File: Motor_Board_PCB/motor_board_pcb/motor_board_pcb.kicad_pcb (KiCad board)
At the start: 2 copper layers, 95 x 45 mm, 110 parts, among them J1 CAN_OUT, J11 CSP-USC16-TR, J2 Screw_Terminal_01x04, J3 Conn_01x02, J4 Screw_Terminal_01x06, J5 Screw_Terminal_01x04, J6 Conn_01x03, J8 Conn_01x02, U1 R7FA4M1AB3CFM, U2 MCP2515-xST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

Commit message: Meeting layout updates
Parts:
- added R34: 0, Resistor_SMD:R_0402_1005Metric, F.Cu at (158.2, 82.8)
- added R35: 0, Resistor_SMD:R_0402_1005Metric, F.Cu at (158.2, 83.9)
- added R36: 0, Resistor_SMD:R_0402_1005Metric, F.Cu at (137.7, 82.0)
- added R7: 0, Resistor_SMD:R_0402_1005Metric, F.Cu at (158.1, 81.2)
- moved TP5 14.3 mm to (131.7, 76.0)
- moved TP13 14.0 mm to (151.2, 88.0)
- moved C14 12.5 mm to (127.1, 90.3)
- moved U3 12.5 mm to (122.0, 90.3)
- moved D11 11.8 mm to (180.8, 74.5)
- moved J8 11.8 mm to (185.3, 77.1)
- moved TP3 10.5 mm to (131.7, 78.0)
- moved TP11 10.0 mm to (149.2, 88.0)
- moved TP2 7.94 mm to (177.1, 72.5)
- moved D6 7.12 mm to (120.9, 79.5)
- moved D7 7.12 mm to (120.8, 76.7)
- moved R17 7.12 mm to (125.1, 79.3)
- moved R18 7.12 mm to (125.0, 76.4)
- moved TP12 6.09 mm to (147.2, 88.0)
- moved C11 3.95 mm to (136.4, 95.7)
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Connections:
- U1 pad 34: D11 -> Net-(U1-CTX0/TDO/SWO/GTIOC1A/P109)
- U1 pad 36: D13 -> Net-(U1-GTIOC3A/P111)
- U1 pad 37: D10 -> Net-(U1-GTIOC3B/P112)
- U2 pad 17: D12 -> Net-(U2-SO)
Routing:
- net +5V: track 237.2 -> 215.9 mm, vias 9 -> 11
- net /CAN/CAN_LOW: track 11.9 -> 24.4 mm
- net /CAN/CAN_HI: track 11.9 -> 24.5 mm
- net D12: track 40.8 -> 29.8 mm
- net D13: track 39.6 -> 29.5 mm
- net D11: track 42.4 -> 32.4 mm
- net D10: track 38.4 -> 31.7 mm
- net VUSB: track 24.5 -> 29.0 mm, vias 2 -> 3
- net Net-(U2-SO): track 0.00 -> 4.25 mm
- net Net-(U1-CTX0/TDO/SWO/GTIOC1A/P109): track 0.00 -> 3.68 mm
- net Net-(U1-GTIOC3A/P111): track 0.00 -> 3.38 mm
- net Net-(U1-GTIOC3B/P112): track 0.00 -> 3.17 mm
- net Net-(D7-K): track 27.8 -> 30.4 mm, vias 2 -> 0
- net USB_D-: track 17.9 -> 19.8 mm
- net USB_D+: track 18.4 -> 19.4 mm
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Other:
- board text added: "FYDP 2024 Group 26 - Ethan Gilbert - Brandon Phu - Jonathon Ko - Ben Flack"

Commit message: Jonathan spelling fix
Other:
- board text added: "FYDP 2024 Group 26 - Ethan Gilbert - Brandon Phu - Jonathan Ko - Ben Flack"
- board text removed: "FYDP 2024 Group 26 - Ethan Gilbert - Brandon Phu - Jonathon Ko - Ben Flack"
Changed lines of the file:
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@@
   (gr_rect (start 92.3 57.9) (end 187.3 102.9)
     (stroke (width 0.1) (type default)) (fill none) (layer "Edge.Cuts"))
-  (gr_text "FYDP 2024\nGroup 26\n- Ethan Gilbert\n- Brandon Phu\n- Jonathon Ko\n- Ben Flack" (at 116.13 100.99) (layer "B.SilkS")
+  (gr_text "FYDP 2024\nGroup 26\n- Ethan Gilbert\n- Brandon Phu\n- Jonathan Ko\n- Ben Flack" (at 116.13 100.99) (layer "B.SilkS")
     (effects (font (size 1.5 1.5) (thickness 0.3) bold) (justify left bottom mirror))
   )

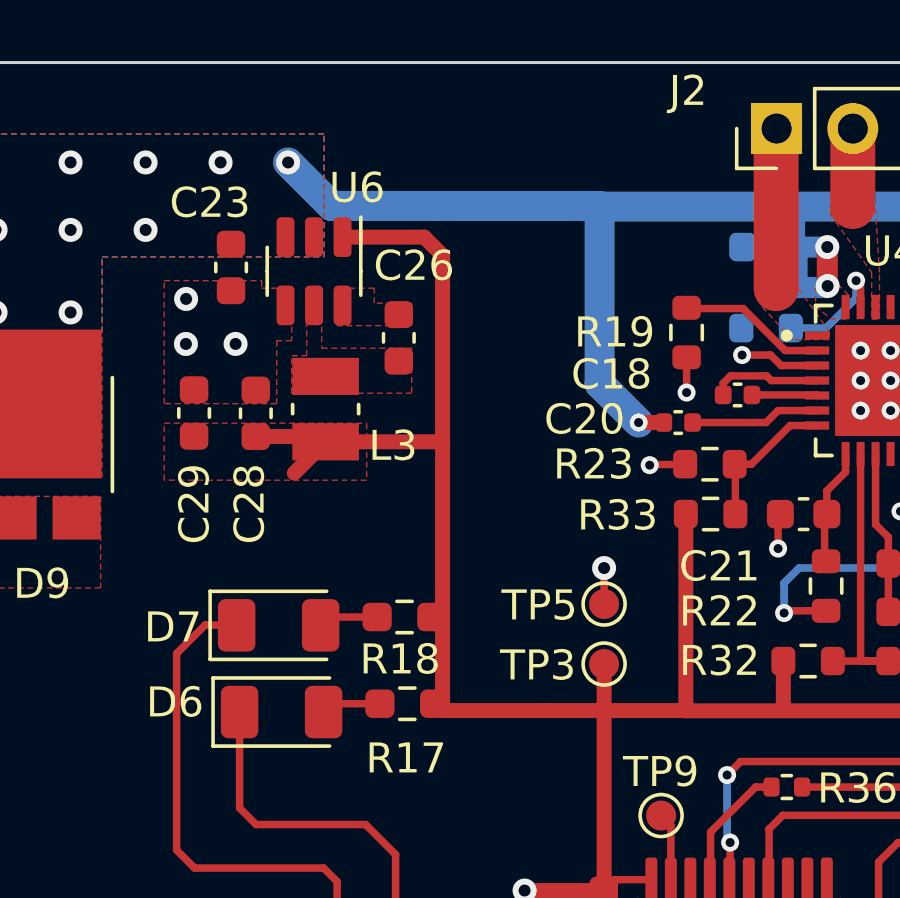
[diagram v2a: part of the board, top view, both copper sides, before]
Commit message: Testpoint location changes
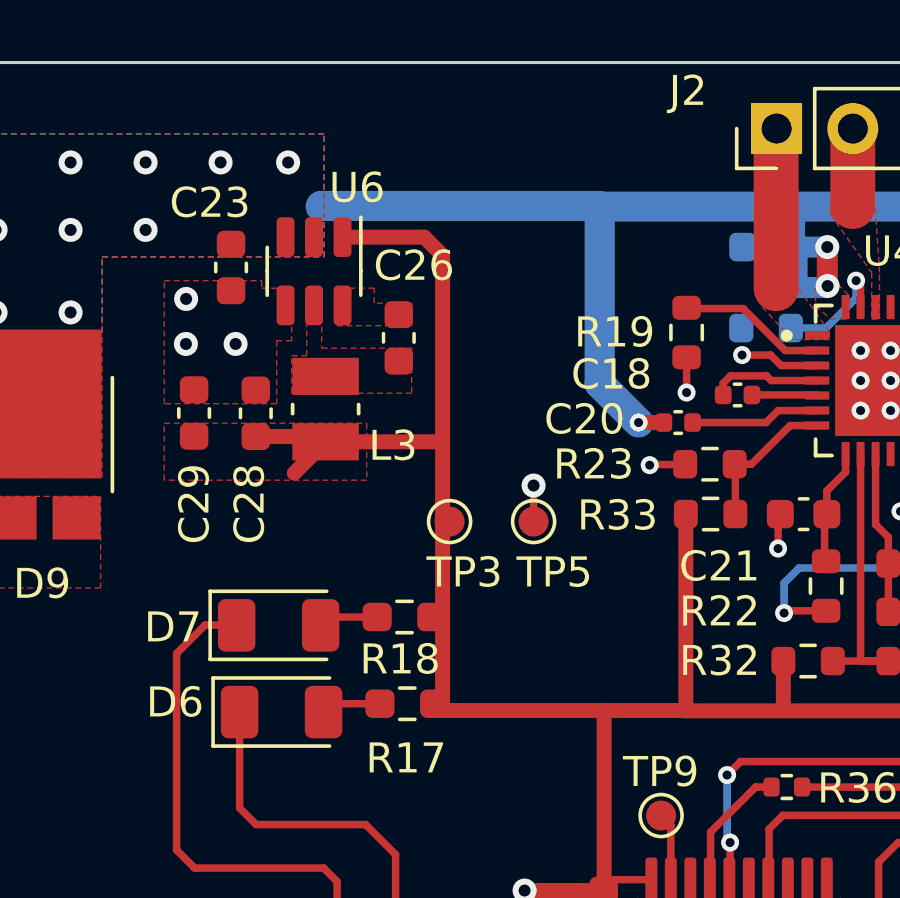
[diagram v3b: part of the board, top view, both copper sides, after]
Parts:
- moved TP3 7.01 mm to (126.5, 73.2)
- moved TP5 3.62 mm to (129.3, 73.2)
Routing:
- net +12V: track 45.8 -> 44.1 mm
- net +5V: track 215.9 -> 214.3 mm
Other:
- board text added: "ECE FYDP 2024 Group 26 - Ethan Gilbert - Brandon Phu - Jonathan Ko - Ben Flack"
- board text removed: "FYDP 2024 Group 26 - Ethan Gilbert - Brandon Phu - Jonathan Ko - Ben Flack"
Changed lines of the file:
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@@
   )
   (footprint "TestPoint:TestPoint_Pad_D1.0mm" (layer "F.Cu")
-    (at 131.65 77.95)
+    (at 126.5 73.2)
     (descr "SMD pad as test Point, diameter 1.0mm")
     (tags "test point SMD pad")
@@
     (property "ki_keywords" "test point tp")
     (attr exclude_from_pos_files)
-    (fp_text reference "TP3" (at -2.2 0.05) (layer "F.SilkS")
+    (fp_text reference "TP3" (at 0.5 1.7) (layer "F.SilkS")
         (effects (font (size 1 1) (thickness 0.16)))
     )
@@
   )
   (footprint "TestPoint:TestPoint_Pad_D1.0mm" (layer "F.Cu")
-    (at 131.65 75.95)
+    (at 129.3 73.2)
     (descr "SMD pad as test Point, diameter 1.0mm")
     (tags "test point SMD pad")
@@
     (property "ki_keywords" "test point tp")
     (attr exclude_from_pos_files)
-    (fp_text reference "TP5" (at -2.15 0.05) (layer "F.SilkS")
+    (fp_text reference "TP5" (at 0.7 1.7) (layer "F.SilkS")
         (effects (font (size 1 1) (thickness 0.16)))
     )
@@
   (gr_rect (start 92.3 57.9) (end 187.3 102.9)
     (stroke (width 0.1) (type default)) (fill none) (layer "Edge.Cuts"))
-  (gr_text "FYDP 2024\nGroup 26\n- Ethan Gilbert\n- Brandon Phu\n- Jonathan Ko\n- Ben Flack" (at 116.13 100.99) (layer "B.SilkS")
+  (gr_text "ECE FYDP 2024\nGroup 26\n- Ethan Gilbert\n- Brandon Phu\n- Jonathan Ko\n- Ben Flack" (at 116.13 100.99) (layer "B.SilkS")
     (effects (font (size 1.5 1.5) (thickness 0.3) bold) (justify left bottom mirror))
   )
@@
   (segment (start 131.625 87.0509) (end 131.6384 87.0375) (width 0.25) (layer "F.Cu") (net 1))
   (segment (start 173.892173 64.76) (end 173.892173 65.821365) (width 0.25) (layer "F.Cu") (net 1))
-  (segment (start 131.65 74.75) (end 131.65 75.95) (width 0.25) (layer "F.Cu") (net 1))
+  (segment (start 129.3 72) (end 129.3 73.2) (width 0.25) (layer "F.Cu") (net 1))
   (segment (start 136.25 67.65) (end 137.2 67.65) (width 0.25) (layer "F.Cu") (net 1))
   (segment (start 175.3 83.2) (end 175.3 82.325) (width 0.25) (layer "F.Cu") (net 1))
@@
   (via (at 141.2 68.5) (size 0.6) (drill 0.3) (layers "F.Cu" "B.Cu") (net 1))
   (via (at 142.2 68.5) (size 0.6) (drill 0.3) (layers "F.Cu" "B.Cu") (net 1))
-  (via (at 131.65 74.75) (size 0.8) (drill 0.4) (layers "F.Cu" "B.Cu") (free) (net 1))
+  (via (at 129.3 72) (size 0.8) (drill 0.4) (layers "F.Cu" "B.Cu") (free) (net 1))
   (via (at 142.2 67.5) (size 0.6) (drill 0.3) (layers "F.Cu" "B.Cu") (net 1))
   (via (at 140.2 68.5) (size 0.6) (drill 0.3) (layers "F.Cu" "B.Cu") (net 1))
@@
   (segment (start 137.85 62.87) (end 138.02 62.7) (width 1) (layer "B.Cu") (net 11))
   (segment (start 137.85 64.025) (end 137.85 62.87) (width 1) (layer "B.Cu") (net 11))
-  (segment (start 131.48 62.68) (end 131.5 62.7) (width 1) (layer "B.Cu") (net 11))
+  (segment (start 122.2 62.7) (end 122.22 62.68) (width 1) (layer "B.Cu") (net 11))
   (segment (start 144.37 64.255) (end 144.625 64) (width 0.7) (layer "B.Cu") (net 11))
+  (segment (start 131.48 62.68) (end 131.5 62.7) (width 1) (layer "B.Cu") (net 11))
+  (segment (start 122.22 62.68) (end 131.48 62.68) (width 1) (layer "B.Cu") (net 11))
   (segment (start 144.575 64.05) (end 144.625 64) (width 0.25) (layer "B.Cu") (net 11))
   (segment (start 139.05 65.4) (end 139.1 65.35) (width 0.25) (layer "B.Cu") (net 11))
@@
   (segment (start 144.37 65.35) (end 144.37 64.255) (width 0.7) (layer "B.Cu") (net 11))
   (segment (start 138.08 64.305) (end 137.825 64.05) (width 0.7) (layer "B.Cu") (net 11))
-  (segment (start 121.116833 61.23) (end 122.566833 62.68) (width 1) (layer "B.Cu") (net 11))
   (segment (start 137.825 64.05) (end 139.09 64.05) (width 0.7) (layer "B.Cu") (net 11))
   (segment (start 138.02 62.7) (end 144.56 62.7) (width 1) (layer "B.Cu") (net 11))
-  (segment (start 122.566833 62.68) (end 131.48 62.68) (width 1) (layer "B.Cu") (net 11))
   (segment (start 144.37 65.35) (end 143.3 65.35) (width 0.7) (layer "B.Cu") (net 11))
   (segment (start 138.08 65.4) (end 139.05 65.4) (width 0.7) (layer "B.Cu") (net 11))
@@
   (segment (start 165.5 98.1) (end 165.6 98) (width 0.5) (layer "F.Cu") (net 18))
   (segment (start 129.75 79.5) (end 134.37 79.5) (width 0.5) (layer "F.Cu") (net 18))
-  (segment (start 131.65 79.5) (end 131.65 77.95) (width 0.5) (layer "F.Cu") (net 18))
   (segment (start 129 89.45) (end 127.19 89.45) (width 0.5) (layer "F.Cu") (net 18))
   (segment (start 131.6384 85.4875) (end 131.65 85.4759) (width 0.5) (layer "F.Cu") (net 18))

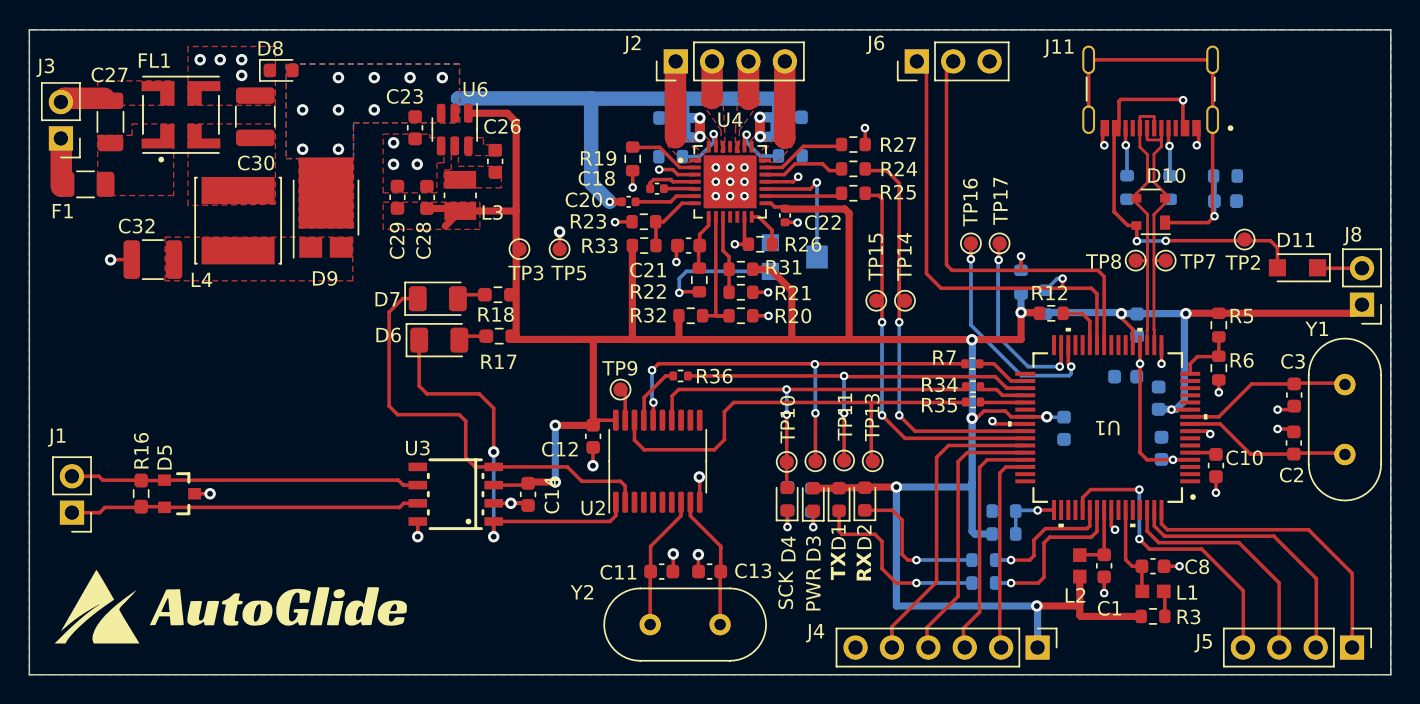
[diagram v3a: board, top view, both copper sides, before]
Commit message: All usb changes on both boards
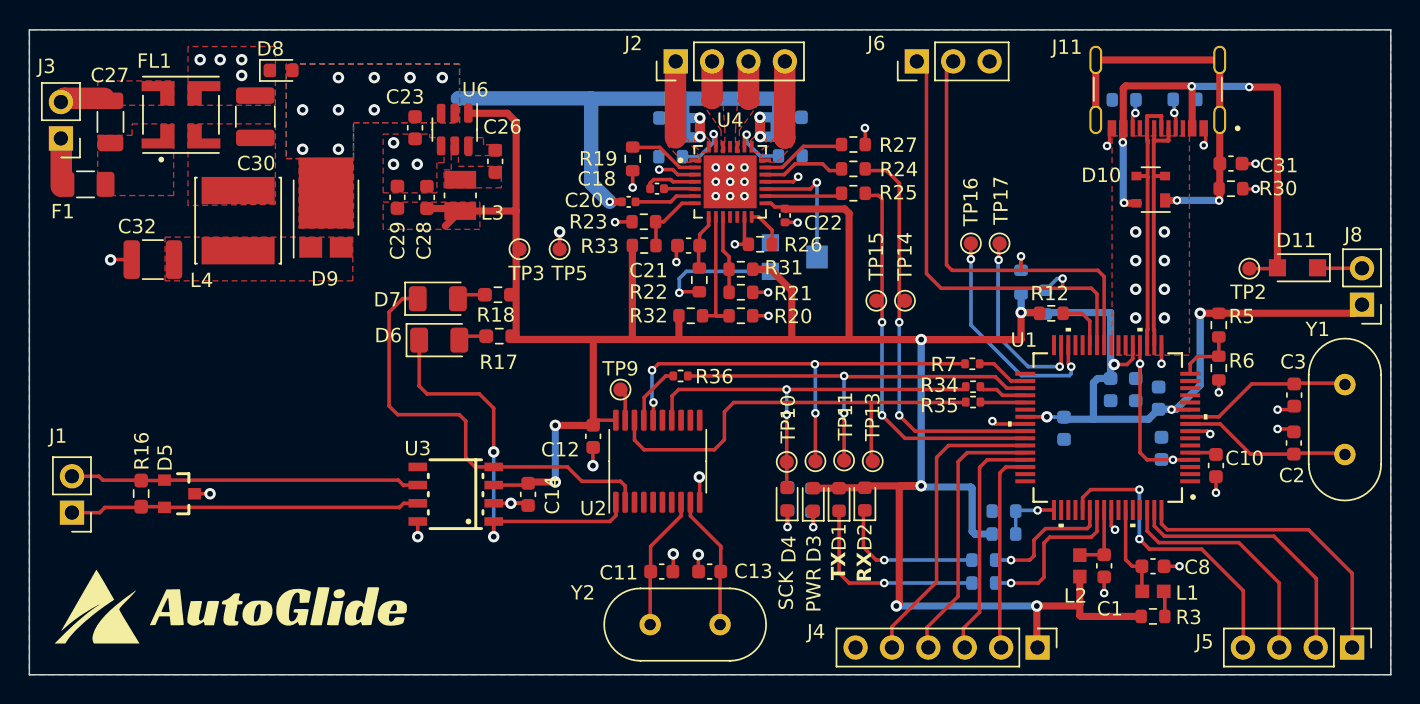
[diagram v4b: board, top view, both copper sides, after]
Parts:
- removed TP7, TP8: TestPoint, TestPoint:TestPoint_Pad_D1.0mm
- C31, R30: moved to F.Cu
- moved R2 6.24 mm to (172.9, 62.8), turned to 0 degrees
- moved R1 6.12 mm to (168.7, 62.8), turned to 180 degrees
- moved C5 4.87 mm to (167.8, 83.0)
- moved C31 2.65 mm to (176.1, 67.2)
- moved TP2 2.06 mm to (177.4, 74.6)
- moved D10 1.55 mm to (170.6, 69.0)
- moved C7 1.14 mm to (169.5, 83.0), turned to 90 degrees
- moved R30 0.96 mm to (176.1, 69.0)
- moved J11 0.50 mm to (171.0, 64.8)
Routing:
- net +5V: track 214.3 -> 224.9 mm
- net VUSB: track 29.0 -> 37.7 mm, vias 3 -> 4
- net /Connectors/SHIELD2: track 29.7 -> 26.4 mm, vias 1 -> 2
- net GND: track 45.4 -> 47.3 mm, vias 47 -> 57
- net USB_D-: track 19.8 -> 17.9 mm
- net CC1: track 3.52 -> 2.09 mm
- net CC2: track 3.37 -> 2.08 mm
- net USB_D+: track 19.4 -> 18.7 mm
- net Net-(D1-K): track 13.4 -> 13.9 mm

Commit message: Kim changes + GND pour + TearDrops + Oscillator changes
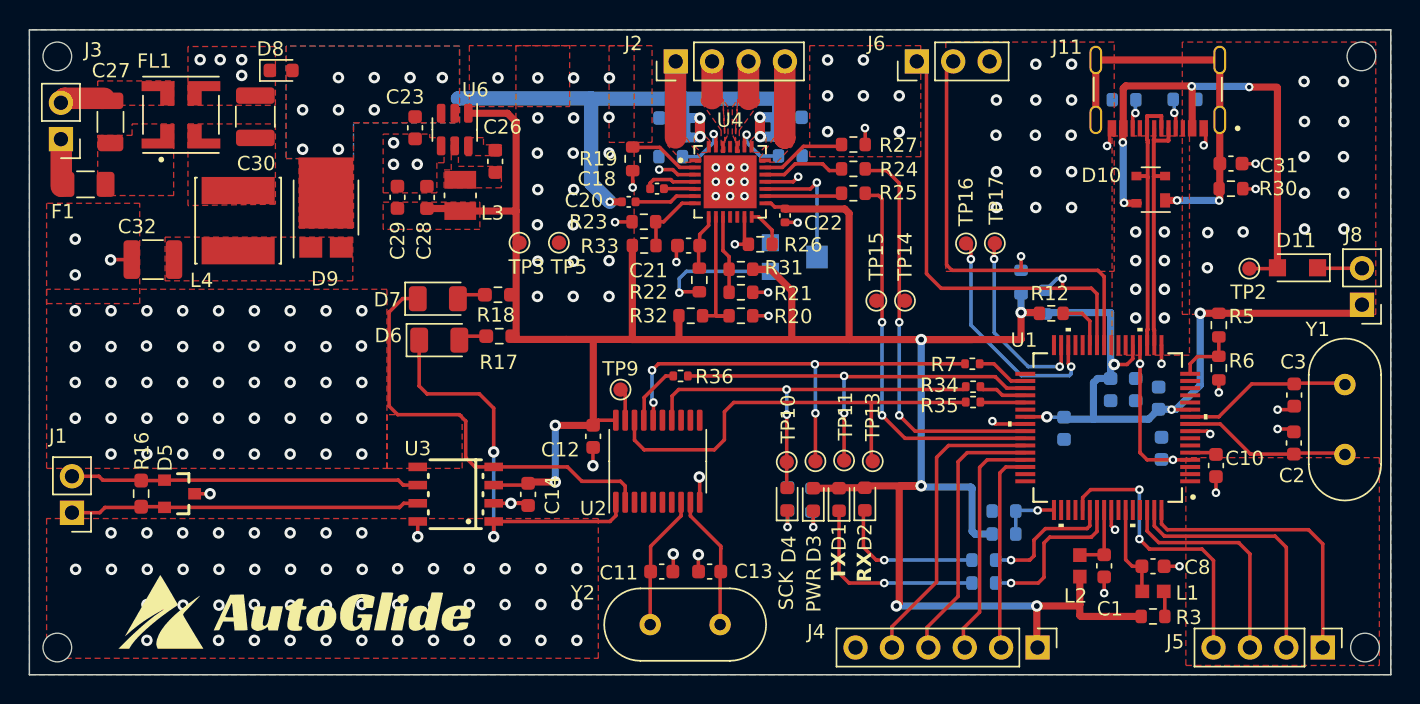
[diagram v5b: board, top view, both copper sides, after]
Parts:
- added ?: , , F.Cu at (94.2, 101.0)
- added ?: , , F.Cu at (185.5, 101.0)
- added ?: , , F.Cu at (185.2, 59.8)
- added ?: , , F.Cu at (94.2, 59.8)
- moved G*** 4.47 mm to (111.0, 98.5)
- moved J5 2.05 mm to (182.6, 101.0)
- moved TP5 0.45 mm to (129.2, 72.8)
- moved TP3 0.45 mm to (126.5, 72.8)
- moved TP16 0.34 mm to (157.7, 72.8)
- moved TP17 0.33 mm to (159.7, 72.8)
- moved J3 0.05 mm to (94.5, 65.5)
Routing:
- net +5V: track 224.9 -> 223.4 mm
- net GND: track 47.3 -> 46.1 mm, vias 57 -> 205

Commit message: minor changes
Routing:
- net GND: vias 205 -> 208
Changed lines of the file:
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@@
   (via (at 174.527307 72.043357) (size 0.8) (drill 0.4) (layers "F.Cu" "B.Cu") (net 86))
   (via (at 139.05 89.1) (size 0.8) (drill 0.4) (layers "F.Cu" "B.Cu") (net 86))
+  (via (at 95.5 98) (size 0.8) (drill 0.4) (layers "F.Cu" "B.Cu") (net 86))
   (via (at 108 85) (size 0.8) (drill 0.4) (layers "F.Cu" "B.Cu") (net 86))
   (via (at 169.5 78) (size 0.8) (drill 0.4) (layers "F.Cu" "B.Cu") (free) (net 86))
@@
   (via (at 104.91 90.27) (size 0.8) (drill 0.4) (layers "F.Cu" "B.Cu") (net 86))
   (via (at 125.9 90.935) (size 0.8) (drill 0.4) (layers "F.Cu" "B.Cu") (net 86))
+  (via (at 98 98) (size 0.8) (drill 0.4) (layers "F.Cu" "B.Cu") (net 86))
   (via (at 107.116833 59.98) (size 0.8) (drill 0.4) (layers "F.Cu" "B.Cu") (net 86))
   (via (at 143.88 77.86) (size 0.6) (drill 0.3) (layers "F.Cu" "B.Cu") (net 86))
@@
   (via (at 184.027307 64.293357) (size 0.8) (drill 0.4) (layers "F.Cu" "B.Cu") (net 86))
   (via (at 184 61.5) (size 0.8) (drill 0.4) (layers "F.Cu" "B.Cu") (net 86))
+  (via (at 98 100.5) (size 0.8) (drill 0.4) (layers "F.Cu" "B.Cu") (net 86))
   (via (at 100.472693 79.956643) (size 0.8) (drill 0.4) (layers "F.Cu" "B.Cu") (net 86))
   (via (at 100.5 100.5) (size 0.8) (drill 0.4) (layers "F.Cu" "B.Cu") (net 86))
@@
   (zone (net 86) (net_name "GND") (layer "F.Cu") (hatch edge 0.5)
     (priority 17)
-    (connect_pads yes (clearance 0.3))
-    (min_thickness 0.3) (filled_areas_thickness no)
+    (connect_pads yes (clearance 0.5))
+    (min_thickness 0.5) (filled_areas_thickness no)
     (fill yes (thermal_gap 0.5) (thermal_bridge_width 0.5))
     (polygon
@@
       (pts
         (xy 100 77)
-        (xy 100 70)
-        (xy 93.5 70)
+        (xy 100 71.5)
+        (xy 93.5 71.5)
         (xy 93.5 77)
       )
